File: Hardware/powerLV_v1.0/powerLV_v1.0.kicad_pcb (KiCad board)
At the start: 2 copper layers, 100 x 100 mm, 4 parts

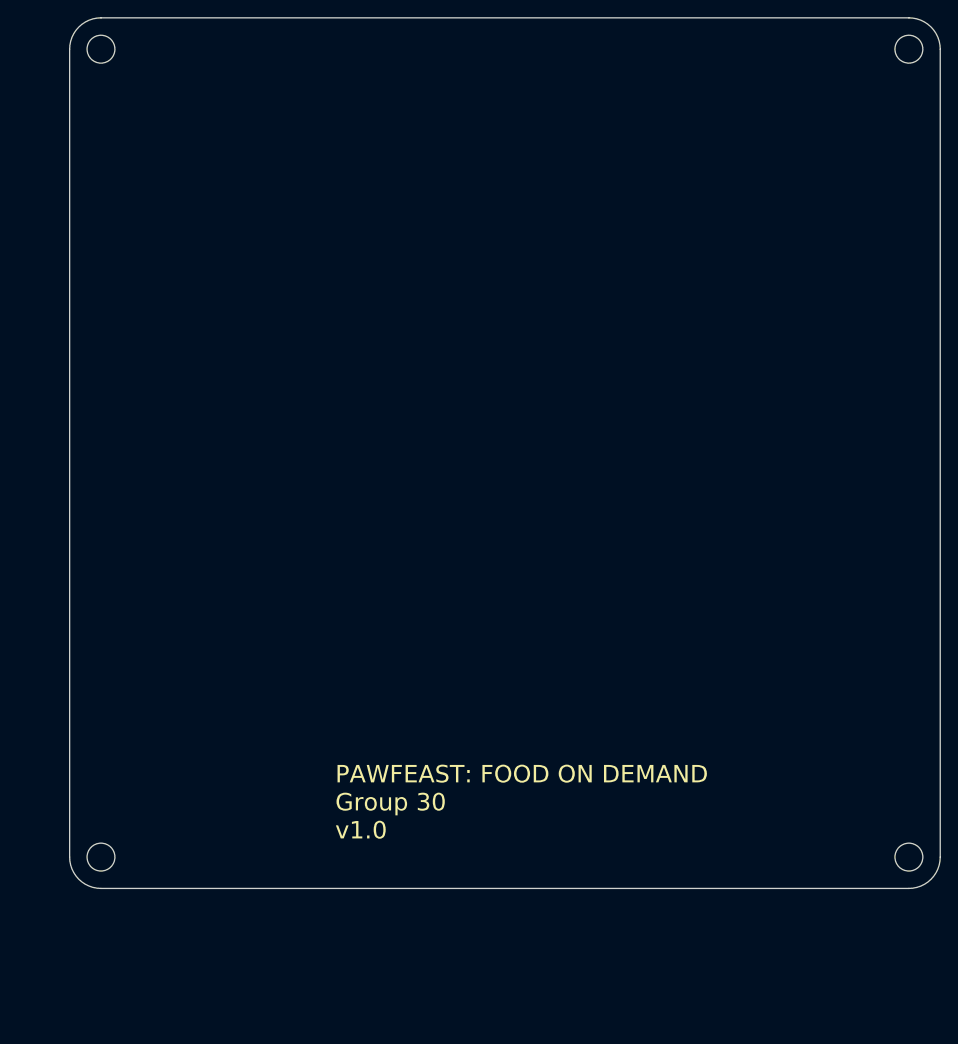
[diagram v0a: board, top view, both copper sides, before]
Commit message: made motor driver layout base and moved brain power to a separate board
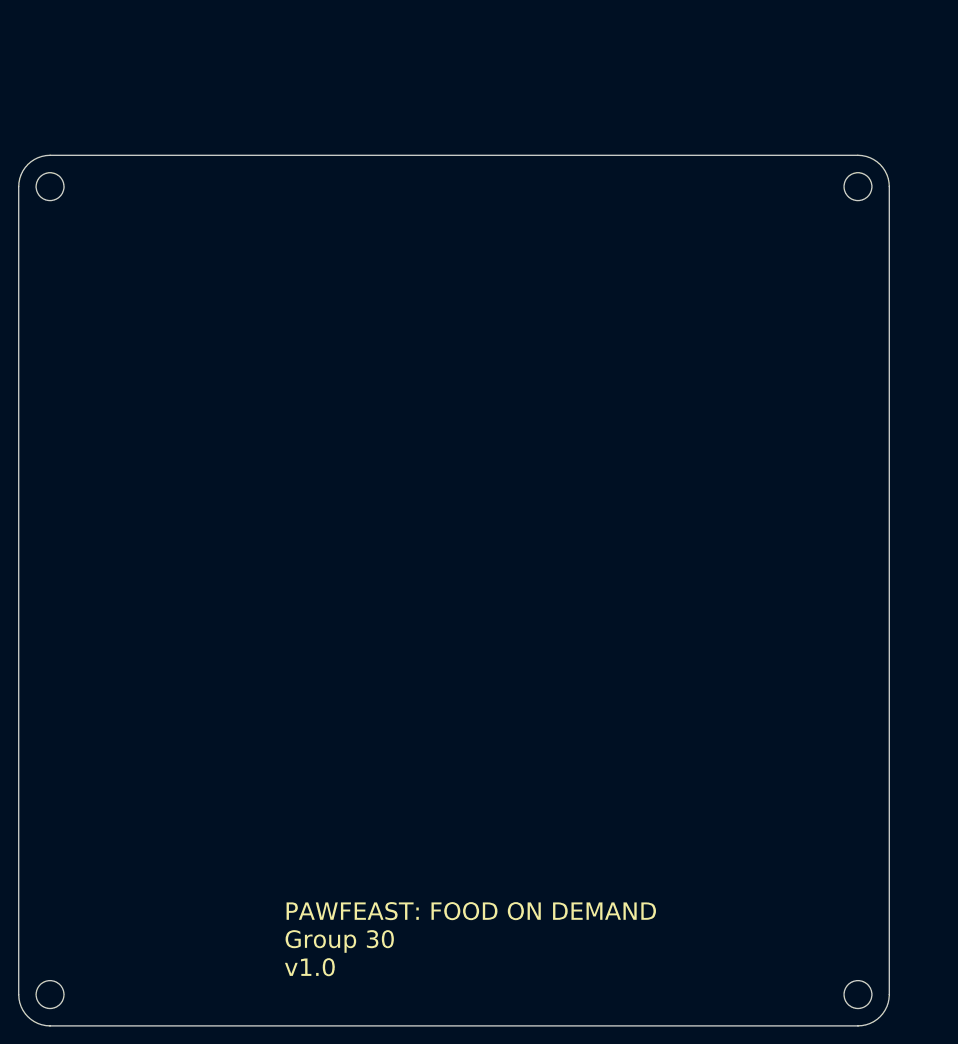
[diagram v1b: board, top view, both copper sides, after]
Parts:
- moved H1 16.8 mm to (83.6, 47.6)
- moved H3 16.8 mm to (83.6, 140.4)
- moved H4 16.8 mm to (176.4, 140.4)
- moved H2 16.8 mm to (176.4, 47.6)
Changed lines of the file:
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@@
   )
   (setup
+    (stackup
+      (layer "F.SilkS" (type "Top Silk Screen"))
+      (layer "F.Paste" (type "Top Solder Paste"))
+      (layer "F.Mask" (type "Top Solder Mask") (thickness 0.01))
+      (layer "F.Cu" (type "copper") (thickness 0.035))
+      (layer "dielectric 1" (type "core") (thickness 1.51) (material "FR4") (epsilon_r 4.5) (loss_tangent 0.02))
+      (layer "B.Cu" (type "copper") (thickness 0.035))
+      (layer "B.Mask" (type "Bottom Solder Mask") (thickness 0.01))
+      (layer "B.Paste" (type "Bottom Solder Paste"))
+      (layer "B.SilkS" (type "Bottom Silk Screen"))
+      (copper_finish "None")
+      (dielectric_constraints no)
+    )
     (pad_to_mask_clearance 0)
     (pcbplotparams
@@
   (net 0 "")
   (footprint "MountingHole:MountingHole_3.2mm_M3" (layer "F.Cu")
-    (at 89.45 31.81)
+    (at 83.6 140.4)
+    (descr "Mounting Hole 3.2mm, no annular, M3")
+    (tags "mounting hole 3.2mm no annular m3")
+    (property "Link" "NA")
+    (property "MPN" "NA")
+    (property "Sheetfile" "power_v1.0.kicad_sch")
+    (property "Sheetname" "")
+    (property "ki_description" "Mounting Hole without connection")
+    (property "ki_keywords" "mounting hole")
+    (attr exclude_from_pos_files)
+    (fp_text reference "H3" (at 0 -4.2) (layer "F.SilkS") hide
+        (effects (font (size 1 1) (thickness 0.15)))
+    )
+    (fp_text value "MountingHole" (at 0 4.2) (layer "F.Fab")
+        (effects (font (size 1 1) (thickness 0.15)))
+    )
+    (fp_text user "${REFERENCE}" (at 0 0) (layer "F.Fab")
+        (effects (font (size 1 1) (thickness 0.15)))
+    )
+    (fp_circle (center 0 0) (end 3.2 0)
+      (stroke (width 0.15) (type solid)) (fill none) (layer "Cmts.User"))
+    (fp_circle (center 0 0) (end 3.45 0)
+      (stroke (width 0.05) (type solid)) (fill none) (layer "F.CrtYd"))
+    (pad "" np_thru_hole circle (at 0 0) (size 3.2 3.2) (drill 3.2) (layers "*.Cu" "*.Mask"))
+  )
+  (footprint "MountingHole:MountingHole_3.2mm_M3" (layer "F.Cu")
+    (at 83.6 47.6)
     (descr "Mounting Hole 3.2mm, no annular, M3")
     (tags "mounting hole 3.2mm no annular m3")
@@
     (fp_circle (center 0 0) (end 3.45 0)
       (stroke (width 0.05) (type solid)) (fill none) (layer "F.CrtYd"))
-    (pad "" np_thru_hole circle (at 0 0) (size 3.2 3.2) (drill 3.2) (layers "F&B.Cu" "*.Mask"))
-  )
-  (footprint "MountingHole:MountingHole_3.2mm_M3" (layer "F.Cu")
-    (at 182.25 124.61)
+    (pad "" np_thru_hole circle (at 0 0) (size 3.2 3.2) (drill 3.2) (layers "*.Cu" "*.Mask"))
+  )
+  (footprint "MountingHole:MountingHole_3.2mm_M3" (layer "F.Cu")
+    (at 176.4 140.4)
     (descr "Mounting Hole 3.2mm, no annular, M3")
     (tags "mounting hole 3.2mm no annular m3")
@@
     (fp_circle (center 0 0) (end 3.45 0)
       (stroke (width 0.05) (type solid)) (fill none) (layer "F.CrtYd"))
-    (pad "" np_thru_hole circle (at 0 0) (size 3.2 3.2) (drill 3.2) (layers "F&B.Cu" "*.Mask"))
-  )
-  (footprint "MountingHole:MountingHole_3.2mm_M3" (layer "F.Cu")
-    (at 89.45 124.61)
-    (descr "Mounting Hole 3.2mm, no annular, M3")
-    (tags "mounting hole 3.2mm no annular m3")
-    (property "Link" "NA")
-    (property "MPN" "NA")
-    (property "Sheetfile" "power_v1.0.kicad_sch")
-    (property "Sheetname" "")
-    (property "ki_description" "Mounting Hole without connection")
-    (property "ki_keywords" "mounting hole")
-    (attr exclude_from_pos_files)
-    (fp_text reference "H3" (at 0 -4.2) (layer "F.SilkS") hide
-        (effects (font (size 1 1) (thickness 0.15)))
-    )
-    (fp_text value "MountingHole" (at 0 4.2) (layer "F.Fab")
-        (effects (font (size 1 1) (thickness 0.15)))
-    )
-    (fp_text user "${REFERENCE}" (at 0 0) (layer "F.Fab")
-        (effects (font (size 1 1) (thickness 0.15)))
-    )
-    (fp_circle (center 0 0) (end 3.2 0)
-      (stroke (width 0.15) (type solid)) (fill none) (layer "Cmts.User"))
-    (fp_circle (center 0 0) (end 3.45 0)
-      (stroke (width 0.05) (type solid)) (fill none) (layer "F.CrtYd"))
-    (pad "" np_thru_hole circle (at 0 0) (size 3.2 3.2) (drill 3.2) (layers "F&B.Cu" "*.Mask"))
-  )
-  (footprint "MountingHole:MountingHole_3.2mm_M3" (layer "F.Cu")
-    (at 182.25 31.81)
+    (pad "" np_thru_hole circle (at 0 0) (size 3.2 3.2) (drill 3.2) (layers "*.Cu" "*.Mask"))
+  )
+  (footprint "MountingHole:MountingHole_3.2mm_M3" (layer "F.Cu")
+    (at 176.4 47.6)
     (descr "Mounting Hole 3.2mm, no annular, M3")
     (tags "mounting hole 3.2mm no annular m3")
@@
     (fp_circle (center 0 0) (end 3.45 0)
       (stroke (width 0.05) (type solid)) (fill none) (layer "F.CrtYd"))
-    (pad "" np_thru_hole circle (at 0 0) (size 3.2 3.2) (drill 3.2) (layers "F&B.Cu" "*.Mask"))
-  )
-  (gr_line (start 185.85 31.81) (end 185.85 124.61)
-    (stroke (width 0.1) (type default)) (layer "Edge.Cuts"))
-  (gr_line (start 89.45 28.21) (end 182.25 28.21)
-    (stroke (width 0.1) (type default)) (layer "Edge.Cuts"))
-  (gr_arc (start 185.85 124.61) (mid 184.795584 127.155584) (end 182.25 128.21)
-    (stroke (width 0.1) (type default)) (layer "Edge.Cuts"))
-  (gr_arc (start 85.85 31.81) (mid 86.904416 29.264416) (end 89.45 28.21)
-    (stroke (width 0.1) (type default)) (layer "Edge.Cuts"))
-  (gr_arc (start 182.25 28.21) (mid 184.795584 29.264416) (end 185.85 31.81)
-    (stroke (width 0.1) (type default)) (layer "Edge.Cuts"))
-  (gr_line (start 182.25 128.21) (end 89.45 128.21)
-    (stroke (width 0.1) (type default)) (layer "Edge.Cuts"))
-  (gr_arc (start 89.45 128.21) (mid 86.904416 127.155584) (end 85.85 124.61)
-    (stroke (width 0.1) (type default)) (layer "Edge.Cuts"))
-  (gr_line (start 85.85 124.61) (end 85.85 31.81)
-    (stroke (width 0.1) (type default)) (layer "Edge.Cuts"))
-  (gr_text "PAWFEAST: FOOD ON DEMAND\nGroup 30\nv1.0" (at 116.35 122.71) (layer "F.SilkS")
+    (pad "" np_thru_hole circle (at 0 0) (size 3.2 3.2) (drill 3.2) (layers "*.Cu" "*.Mask"))
+  )
+  (gr_arc (start 80 47.6) (mid 81.054416 45.054416) (end 83.6 44)
+    (stroke (width 0.1) (type default)) (layer "Edge.Cuts"))
+  (gr_line (start 80 140.4) (end 80 47.6)
+    (stroke (width 0.1) (type default)) (layer "Edge.Cuts"))
+  (gr_arc (start 176.4 44) (mid 178.945584 45.054416) (end 180 47.6)
+    (stroke (width 0.1) (type default)) (layer "Edge.Cuts"))
+  (gr_line (start 176.4 144) (end 83.6 144)
+    (stroke (width 0.1) (type default)) (layer "Edge.Cuts"))
+  (gr_line (start 180 47.6) (end 180 140.4)
+    (stroke (width 0.1) (type default)) (layer "Edge.Cuts"))
+  (gr_arc (start 180 140.4) (mid 178.945584 142.945584) (end 176.4 144)
+    (stroke (width 0.1) (type default)) (layer "Edge.Cuts"))
+  (gr_line (start 83.6 44) (end 176.4 44)
+    (stroke (width 0.1) (type default)) (layer "Edge.Cuts"))
+  (gr_arc (start 83.6 144) (mid 81.054416 142.945584) (end 80 140.4)
+    (stroke (width 0.1) (type default)) (layer "Edge.Cuts"))
+  (gr_text "PAWFEAST: FOOD ON DEMAND\nGroup 30\nv1.0" (at 110.5 138.5) (layer "F.SilkS")
     (effects (font (size 2 2) (thickness 0.3)) (justify left bottom))
   )
   (dimension (type orthogonal) (layer "Dwgs.User")
-    (pts (xy 85.85 28.21) (xy 185.85 28.21))
+    (pts (xy 80 44) (xy 80 144))
+    (height -9.5)
+    (orientation 1)
+    (gr_text "100.0000 mm" (at 69.35 94 90) (layer "Dwgs.User")
+      (effects (font (size 1 1) (thickness 0.15)))
+    )
+    (format (prefix "") (suffix "") (units 3) (units_format 1) (precision 4))
+    (style (thickness 0.15) (arrow_length 1.27) (text_position_mode 0) (extension_height 0.58642) (extension_offset 0.5) keep_text_aligned)
+  )
+  (dimension (type orthogonal) (layer "Dwgs.User")
+    (pts (xy 80 44) (xy 180 44))
     (height -9.5)
     (orientation 0)
-    (gr_text "100.0000 mm" (at 135.85 17.56) (layer "Dwgs.User")
+    (gr_text "100.0000 mm" (at 130 33.35) (layer "Dwgs.User")
       (effects (font (size 1 1) (thickness 0.15)))
     )
@@
   )
   (dimension (type orthogonal) (layer "Dwgs.User")
-    (pts (xy 85.85 28.21) (xy 85.85 128.21))
-    (height -9.5)
-    (orientation 1)
-    (gr_text "100.0000 mm" (at 75.2 78.21 90) (layer "Dwgs.User")
+    (pts (xy 80 144) (xy 180 144))
+    (height 11)
+    (orientation 0)
+    (gr_text "100.0000 mm" (at 130 153.85) (layer "Dwgs.User")
       (effects (font (size 1 1) (thickness 0.15)))
     )
@@
   )
   (dimension (type orthogonal) (layer "Dwgs.User")
-    (pts (xy 185.85 28.21) (xy 185.85 128.21))
+    (pts (xy 180 44) (xy 180 144))
     (height 12)
     (orientation 1)
-    (gr_text "100.0000 mm" (at 196.7 78.21 90) (layer "Dwgs.User")
-      (effects (font (size 1 1) (thickness 0.15)))
-    )
-    (format (prefix "") (suffix "") (units 3) (units_format 1) (precision 4))
-    (style (thickness 0.15) (arrow_length 1.27) (text_position_mode 0) (extension_height 0.58642) (extension_offset 0.5) keep_text_aligned)
-  )
-  (dimension (type orthogonal) (layer "Dwgs.User")
-    (pts (xy 85.85 128.21) (xy 185.85 128.21))
-    (height 11)
-    (orientation 0)
-    (gr_text "100.0000 mm" (at 135.85 138.06) (layer "Dwgs.User")
-      (effects (font (size 1 1) (thickness 0.15)))
-    )
+    (gr_text "100.0000 mm" (at 190.85 94 90) (layer "Dwgs.User")
+      (effects (font (size 1 1) (thickness 0.15)))
+    )

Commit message: instead of an onboard power, I decided to make a separate board for just brain power--essentially a second power board.
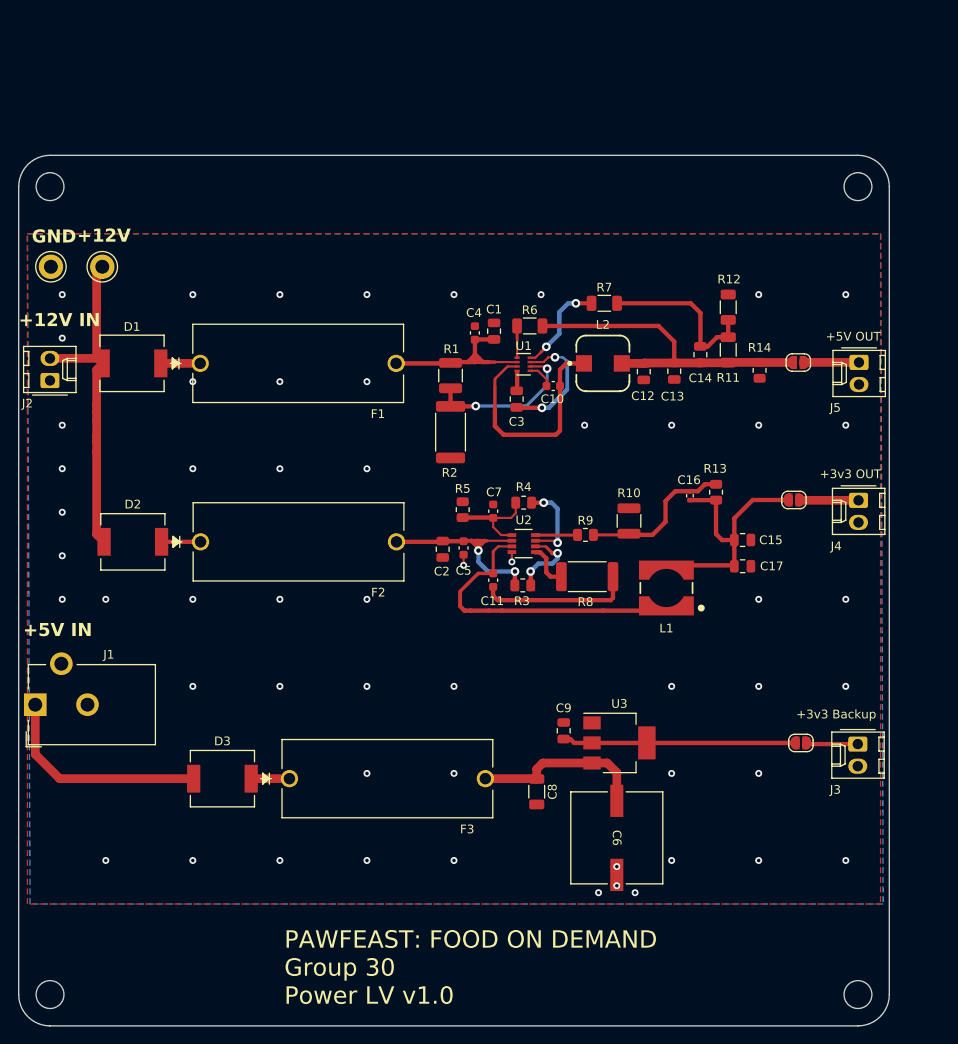
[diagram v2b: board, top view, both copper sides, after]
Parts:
- added C1: 22uF, Capacitor_SMD:C_0805_2012Metric, F.Cu at (134.6, 64.2)
- added C10: 0.1uF, Capacitor_SMD:C_0603_1608Metric, F.Cu at (141.4, 70.5)
- added C11: 0.1uF, Capacitor_SMD:C_0603_1608Metric, F.Cu at (134.5, 92.8)
- added C12: 22uF, Capacitor_SMD:C_0805_2012Metric, F.Cu at (151.8, 68.8)
- added C13: 22uF, Capacitor_SMD:C_0805_2012Metric, F.Cu at (155.3, 68.8)
- added C14: 300pF, Capacitor_SMD:C_0805_2012Metric, F.Cu at (158.3, 66.9)
- added C15: 22uF, Capacitor_SMD:C_0805_2012Metric, F.Cu at (163.2, 88.2)
- added C16: 33pF, Resistor_SMD:R_0402_1005Metric, F.Cu at (157.1, 83.1)
- added C17: 22uF, Capacitor_SMD:C_0805_2012Metric, F.Cu at (163.2, 91.2)
- added C2: 22uF, Capacitor_SMD:C_0805_2012Metric, F.Cu at (128.7, 89.2)
- added C3: 22nF, Capacitor_SMD:C_0805_2012Metric, F.Cu at (137.2, 72.0)
- added C4: 0.1uF, Capacitor_SMD:C_0603_1608Metric, F.Cu at (132.4, 64.4)
- added C5: 0.1uF, Capacitor_SMD:C_0603_1608Metric, F.Cu at (131.1, 89.1)
- added C6: 1000uF, PCG1A102MCL1GS:CAP_PC_10X12P7_NCH, F.Cu at (148.7, 122.4)
- added C7: 0.1uF, Capacitor_SMD:C_0603_1608Metric, F.Cu at (134.5, 84.9)
- added C8: 10uF, Resistor_SMD:R_1206_3216Metric, F.Cu at (139.5, 117.1)
- added C9: 22uF, Capacitor_SMD:C_0805_2012Metric, F.Cu at (142.6, 110.1)
- added D1: D_Schottky, VS_30BQ015_M3_9AT:VS_30BQ015_M3_9AT, F.Cu at (93.0, 67.9)
- added D2: D_Schottky, VS_30BQ015_M3_9AT:VS_30BQ015_M3_9AT, F.Cu at (93.1, 88.4)
- added D3: D_Schottky, VS_30BQ015_M3_9AT:VS_30BQ015_M3_9AT, F.Cu at (103.4, 115.6)
- added F1: Fuse, 4628:FUSE_4628, F.Cu at (112.1, 67.9)
- added F2: Fuse, 4628:FUSE_4628, F.Cu at (112.1, 88.4)
- added F3: Fuse, 4628:FUSE_4628, F.Cu at (122.3, 115.6)
- added J1: Barrel_Jack, Connector_BarrelJack:BarrelJack_CUI_PJ-102AH_Horizontal, F.Cu at (81.9, 107.1)
- added J2: 12V IN, Connector_Molex:Molex_KK-254_AE-6410-02A_1x02_P2.54mm_Vertical, F.Cu at (83.6, 69.9)
- added J3: 3v3 Backup, Connector_Molex:Molex_KK-254_AE-6410-02A_1x02_P2.54mm_Vertical, F.Cu at (176.4, 111.6)
- added J4: 3v3, Connector_Molex:Molex_KK-254_AE-6410-02A_1x02_P2.54mm_Vertical, F.Cu at (176.5, 83.6)
- added J5: 5V OUT, Connector_Molex:Molex_KK-254_AE-6410-02A_1x02_P2.54mm_Vertical, F.Cu at (176.5, 67.8)
- added JP1: SolderJumper_2_Open, Jumper:SolderJumper-2_P1.3mm_Open_RoundedPad1.0x1.5mm, F.Cu at (169.8, 111.5)
- added JP2: SolderJumper_2_Open, Jumper:SolderJumper-2_P1.3mm_Open_RoundedPad1.0x1.5mm, F.Cu at (169.1, 83.6)
- added JP3: SolderJumper_2_Open, Jumper:SolderJumper-2_P1.3mm_Open_RoundedPad1.0x1.5mm, F.Cu at (169.6, 67.8)
- added L1: 4.2uH, 744053004:WE-TPC_5828, F.Cu at (154.4, 93.7)
- added L2: 6.8uH, 7447786006:WE-PD_6050R, F.Cu at (147.1, 67.9)
- added R1: 191k, Resistor_SMD:R_1210_3225Metric, F.Cu at (129.6, 69.3)
- added R10: 12.7k, Resistor_SMD:R_1210_3225Metric, F.Cu at (150.1, 86.0)
- added R11: 90.9k, Resistor_SMD:R_1206_3216Metric, F.Cu at (161.5, 66.3)
- added R12: 10k, Resistor_SMD:R_1206_3216Metric, F.Cu at (161.5, 61.5)
- added R13: 40.2k, Resistor_SMD:R_0805_2012Metric, F.Cu at (160.1, 82.7)
- added R14: 100k, Resistor_SMD:R_0805_2012Metric, F.Cu at (165.1, 68.7)
- added R2: 49.9k, Resistor_SMD:R_2512_6332Metric, F.Cu at (129.6, 75.8)
- added R3: 499k, Resistor_SMD:R_0805_2012Metric, F.Cu at (137.9, 93.4)
- added R4: 100k, Resistor_SMD:R_0805_2012Metric, F.Cu at (138.0, 83.9)
- added R5: 7.5k, Resistor_SMD:R_0805_2012Metric, F.Cu at (131.0, 84.7)
- added R6: 10k, Resistor_SMD:R_1206_3216Metric, F.Cu at (138.7, 63.6)
- added R7: 10k, Resistor_SMD:R_1206_3216Metric, F.Cu at (147.3, 61.0)
- added R8: 10, Resistor_SMD:R_2512_6332Metric, F.Cu at (145.3, 92.4)
- added R9: 33k, Resistor_SMD:R_0805_2012Metric, F.Cu at (145.1, 87.6)
- added TP1: 12V, TestPoint:TestPoint_Keystone_5010-5014_Multipurpose, F.Cu at (89.6, 56.8)
- added TP2: GND, TestPoint:TestPoint_Keystone_5010-5014_Multipurpose, F.Cu at (83.7, 56.8)
- added U1: MP2338GTL-Z, MP2338GTL-Z:SOT583_MP2338_MNP, F.Cu at (138.0, 68.0)
- added U2: MP2315SGJ-Z, MP2315SGJ-Z:TSOT23-8_MP2315S_MNP, F.Cu at (138.0, 88.6)
- added U3: AMS1117-3.3, Package_TO_SOT_SMD:SOT-223-3_TabPin2, F.Cu at (149.0, 111.5)
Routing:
- net +12V: track 0.00 -> 39.3 mm
- net Net-(JP3-A): track 0.00 -> 38.0 mm
- net Net-(U2-SW): track 0.00 -> 35.1 mm
- net Net-(JP2-A): track 0.00 -> 29.7 mm
- net Net-(JP1-A): track 0.00 -> 26.8 mm
- net Net-(U1-SW): track 0.00 -> 26.6 mm
- net +5V: track 0.00 -> 25.1 mm
- net Net-(U2-IN): track 0.00 -> 24.9 mm, vias 0 -> 2
- net /VIN: track 0.00 -> 21.8 mm
- net Net-(U3-VI): track 0.00 -> 20.2 mm
- net Net-(C14-Pad2): track 0.00 -> 19.5 mm
- net Net-(U1-EN): track 0.00 -> 18.1 mm, vias 0 -> 2
- net Net-(C16-Pad1): track 0.00 -> 18.1 mm
- net Net-(C11-Pad1): track 0.00 -> 17.5 mm
- net Net-(U1-SS): track 0.00 -> 14.6 mm, vias 0 -> 2
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- added copper zone on B.Cu, net GND
- added copper zone on F.Cu, net GND
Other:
- board text added: "+12V"
- board text added: "+12V IN"
- board text added: "+3v3 Backup"
- board text added: "+3v3 OUT"
- board text added: "+5V IN"
- board text added: "+5V OUT"
- board text added: "GND"
- board text added: "PAWFEAST: FOOD ON DEMAND Group 30 Power LV v1.0"
- board text removed: "PAWFEAST: FOOD ON DEMAND Group 30 v1.0"
